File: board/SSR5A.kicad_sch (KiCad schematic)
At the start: 20 parts, among them U1 PAN2110P0AA, U2 HLK-PM03, U3 PY32F030K1xTx, X1 SWD, Y1 16MHz

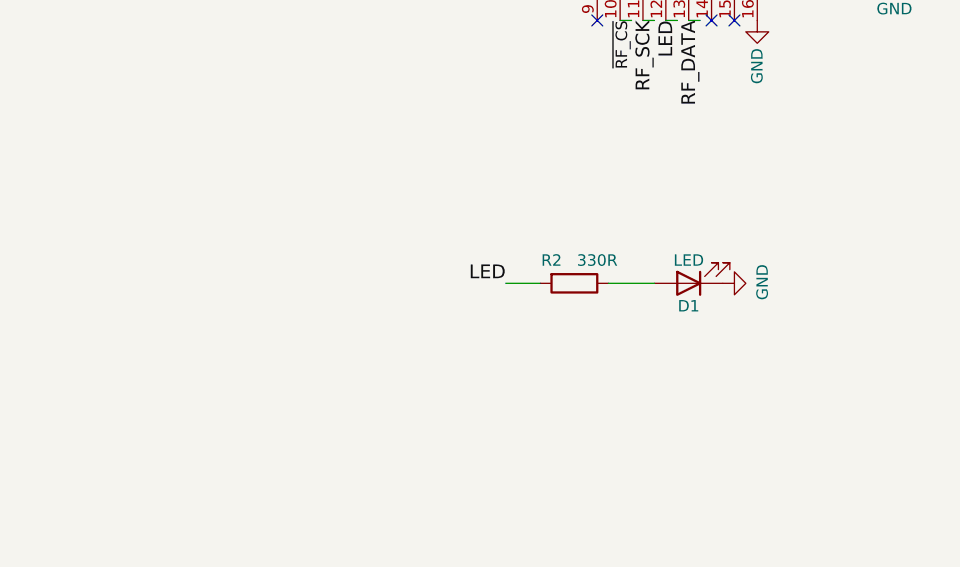
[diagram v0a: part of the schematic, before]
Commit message: Add RGB status LED to SSR5A
Co-authored-by: Copilot <223556219+Copilot@users.noreply.github.com>
Copilot-Session: 109a56b3-5fb8-400b-b74c-480b8f593743
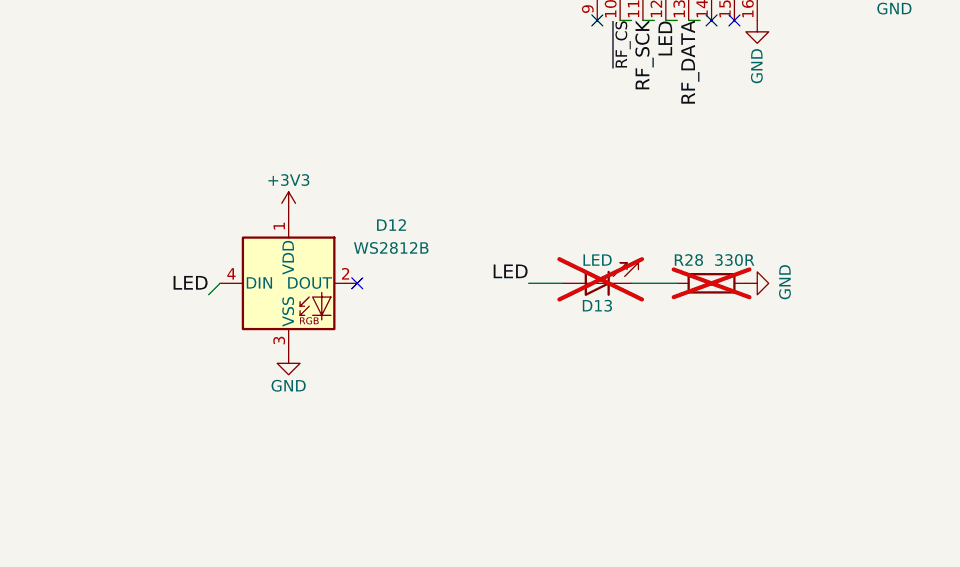
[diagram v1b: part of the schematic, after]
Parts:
- removed D1: LED, LED_SMD:LED_0805_2012Metric_Pad1.15x1.40mm_HandSolder, symbol Device:LED
- removed R2: 330R, Resistor_SMD:R_0805_2012Metric, symbol Device:R
- added D12: WS2812B, LED_SMD:LED_WS2812B_PLCC4_5.0x5.0mm_P3.2mm, symbol LED:WS2812B
- added D13: LED, LED_SMD:LED_0805_2012Metric_Pad1.15x1.40mm_HandSolder, symbol Device:LED
- added R28: 330R, Resistor_SMD:R_0805_2012Metric, symbol Device:R
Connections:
- net +3V3: now also D12.1 (VDD)
- net GND: now also D12.3 (VSS), R28.1
- net LED: now also D12.4 (DIN), D13.2 (A)
- new net: D13.1 (K), R28.2
- no-connect marks 16 -> 17
